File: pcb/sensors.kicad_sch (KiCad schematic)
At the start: 12 parts, among them J2 Conn_01x04_Pin, Q1 BSS138, Q2 BSS138, U3 BME280, U4 SGP30-2.5K

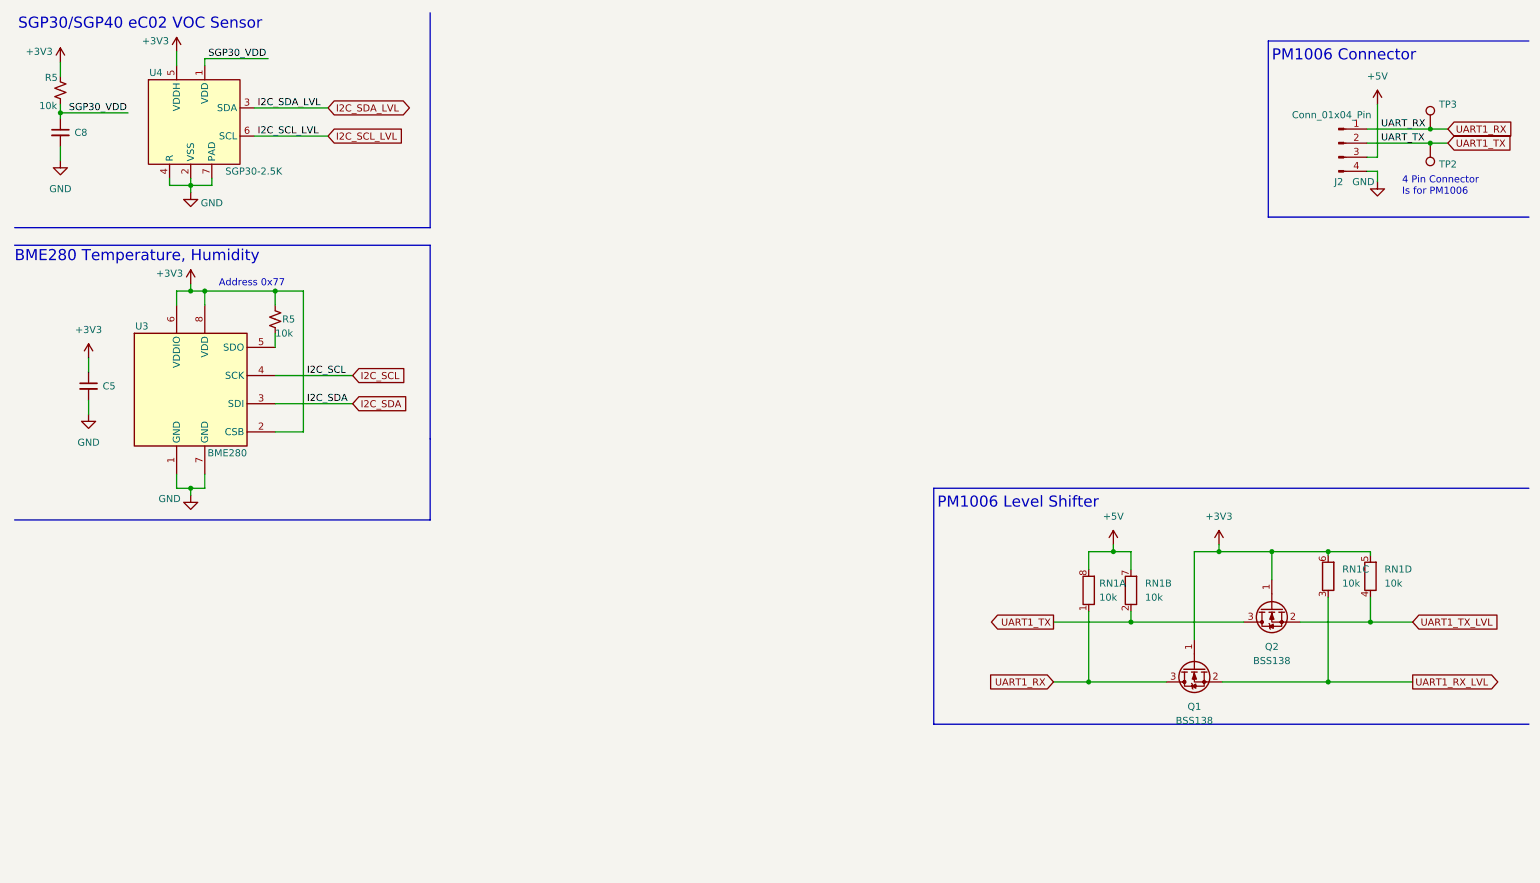
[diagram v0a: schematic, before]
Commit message: finish the routing need to move the esp32 up 5.5 mm
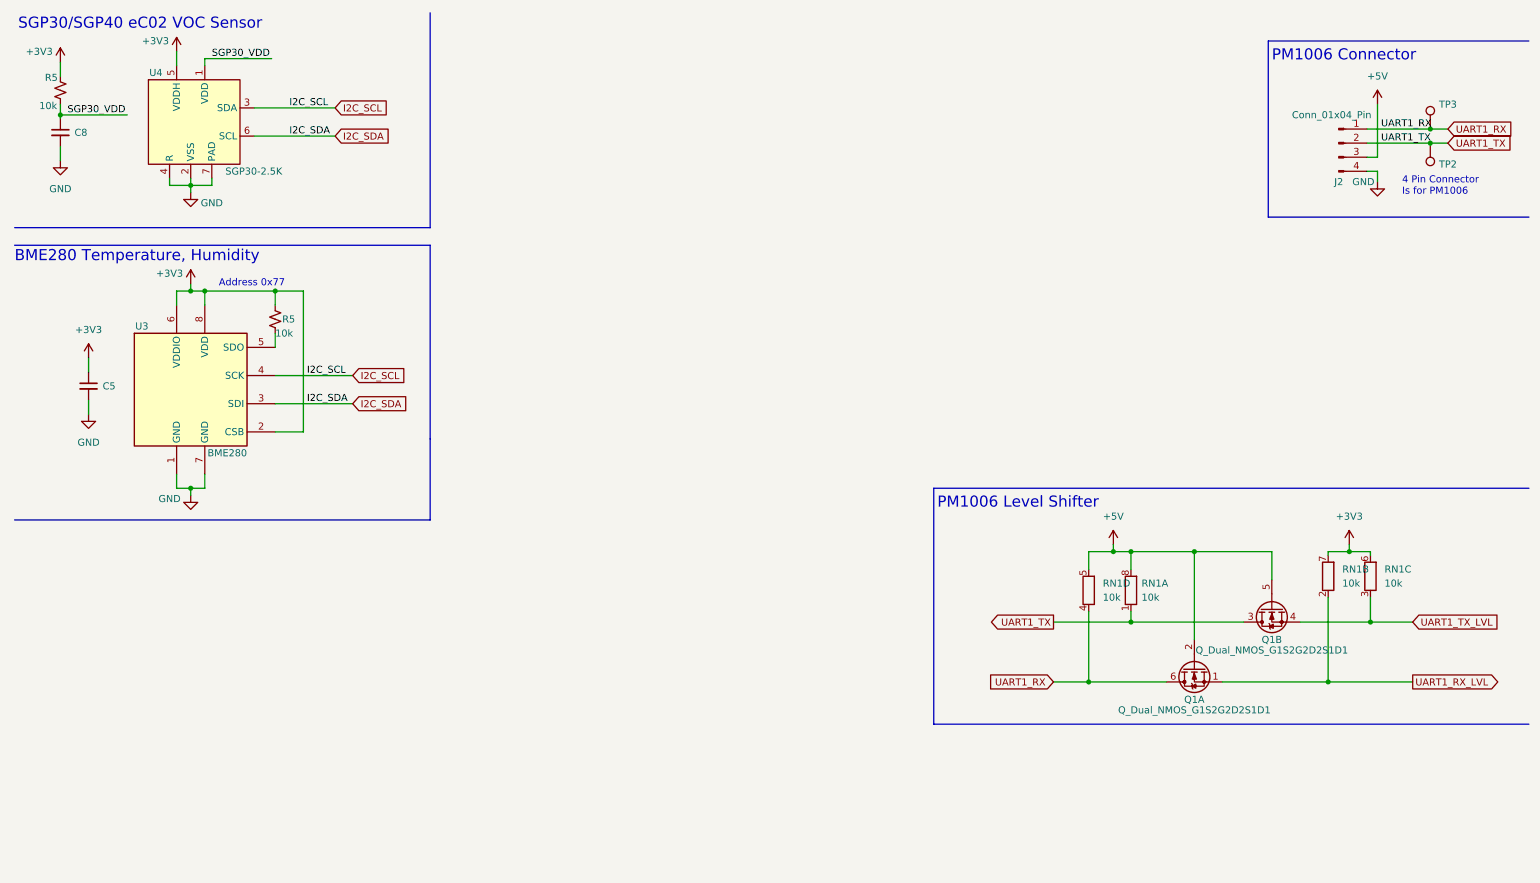
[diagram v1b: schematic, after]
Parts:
- removed Q1, Q2: BSS138, Package_TO_SOT_SMD:SOT-23, symbol Transistor_FET:BSS138
- added Q1: Q_Dual_NMOS_G1S2G2D2S1D1, Package_TO_SOT_SMD:SOT-363_SC-70-6, symbol Kevin_Lutzer_Lbr:Q_Dual_NMOS_BSS138PS
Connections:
- net I2C_SCL_LVL is gone; now on net I2C_SDA: U4.6 (SCL)
- net I2C_SDA_LVL is gone; now on net I2C_SCL: U4.3 (SDA)
- net +3V3: now also RN1.7 (R2.2); no longer RN1.5 (R4.2)
- net +5V: now also RN1.5 (R4.2), Q1.2 (G), Q1.5 (G); no longer RN1.7 (R2.2)
- net UART1_RX: now also RN1.4 (R4.1), Q1.6 (D); no longer RN1.1 (R1.1)
- net UART1_RX_LVL: now also RN1.2 (R2.1), Q1.1 (S); no longer RN1.3 (R3.1)
- net UART1_TX: now also RN1.1 (R1.1), Q1.3 (D); no longer RN1.2 (R2.1)
- net UART1_TX_LVL: now also RN1.3 (R3.1), Q1.4 (S); no longer RN1.4 (R4.1)
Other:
- moved on the sheet: RN1A, RN1B, RN1C, RN1D

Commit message: finish routing the PCB
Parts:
- U4: footprint Kevin_Lutzer_Lbr:SGP30-2.5K_SEN-M -> Kevin_Lutzer_Lbr:SGP30-2.5K_SEN
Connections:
- net +3V3: now also Q1.2 (G), Q1.5 (G)
- net +5V: no longer Q1.2 (G), Q1.5 (G)
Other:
- moved on the sheet: J2, Q1A, Q1B, RN1A, RN1B, RN1C, RN1D, TP2, TP3

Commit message: finish v4 and the images for doucmentation
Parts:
- removed Q1: Q_Dual_NMOS_G1S2G2D2S1D1, Package_TO_SOT_SMD:SOT-363_SC-70-6, symbol Kevin_Lutzer_Lbr:Q_Dual_NMOS_BSS138PS
- removed RN1: 10k, Resistor_SMD:R_Array_Concave_4x0603, symbol Device:R_Pack04_Split
- added C8: 0u1, Capacitor_SMD:C_0603_1608Metric, symbol Device:C_Small
- added D6: D_Photo, Diode_SMD:D_1206_3216Metric_Pad1.42x1.75mm_HandSolder, symbol Device:D_Photo
- added Q1: BSS138, Package_TO_SOT_SMD:SOT-23, symbol Transistor_FET:BSS138
- added R14: R_Small_US, Resistor_SMD:R_0603_1608Metric, symbol Device:R_Small_US
- added R5 (x2): 10k, Resistor_SMD:R_0603_1608Metric, symbol Device:R_Small_US
- added R5 (x2): 2k2, Resistor_SMD:R_0603_1608Metric, symbol Device:R_Small_US
- added R5 (x2): 0, Resistor_SMD:R_0603_1608Metric, symbol Device:R_Small_US
- C5, C8: value 100n -> 0u1
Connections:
- net +3V3: now also C8.1, Q1.1 (G), R14.2, R5.1, R5.2, R5.2
- net +5V: now also R5.1
- net GND: now also C8.2, D6.1 (K)
- net I2C_SCL: now also R5.1
- net I2C_SDA: now also R5.1
- net UART1_RX: now also R5.2; no longer J2.1 (Pin_1), TP3.1
- net UART1_TX: now also Q1.3 (D), R5.2, R5.2; no longer J2.2 (Pin_2), TP2.1
- net UART1_TX_LVL: now also Q1.2 (S), R5.2
- new net: J2.1 (Pin_1), R5.1, TP3.1
- new net: J2.2 (Pin_2), R5.1, TP2.1
- new net PD: D6.2 (A), R14.1
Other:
- note added: "For room reasons I only level shifted the TX signal so it can meet the 4.5V TTL Level of the sensor."
- note added: "I2C Pullups"
- note added: "Photo Diode"
- moved on the sheet: C8, R5, TP2, TP3

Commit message: cleanup undeeded pdf files and add gerbers
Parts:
- added C6: 1u, Capacitor_SMD:C_0603_1608Metric, symbol Device:C_Small
- J2: footprint Connector_JST:JST_ZE_BM04B-ZESS-TBT_1x04-1MP_P1.50mm_Vertical -> Kevin_Lutzer_Lbr:CONN_B4B-ZR-SM4-TF_JST
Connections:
- net +5V: now also C6.1
- net GND: now also C6.2
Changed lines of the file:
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@@
+    (stroke (width 0) (type default))
+  )
+  (wire (pts (xy 97.79 31.115) (xy 97.79 34.925))
     (stroke (width 0) (type default))
   )
@@
   )
   (wire (pts (xy 102.87 97.79) (xy 102.87 99.06))
+    (stroke (width 0) (type default))
+  )
+  (wire (pts (xy 97.79 23.495) (xy 97.79 26.035))
     (stroke (width 0) (type default))
   )
@@
     )
   )
+  (symbol (lib_id "power:+5V") (at 97.79 23.495 0) (unit 1)
+    (in_bom yes) (on_board yes) (dnp no) (fields_autoplaced)
+    (property "Reference" "#PWR033" (at 97.79 27.305 0)
+      (effects (font (size 1.27 1.27)) hide)
+    )
+    (property "Value" "+5V" (at 97.79 18.415 0)
+      (effects (font (size 1.27 1.27)))
+    )
+    (property "Footprint" "" (at 97.79 23.495 0)
+      (effects (font (size 1.27 1.27)) hide)
+    )
+    (property "Datasheet" "" (at 97.79 23.495 0)
+      (effects (font (size 1.27 1.27)) hide)
+    )
+    (pin "1")
+    (instances
+      (project "room_environment_monitor"
+        (path "/44f2386d-4dcf-411b-99dd-82c40d92c146"
+          (reference "#PWR033") (unit 1)
+        )
+        (path "/44f2386d-4dcf-411b-99dd-82c40d92c146/789efca6-28c5-460e-8523-846d22f060e4"
+          (reference "#PWR038") (unit 1)
+        )
+      )
+    )
+  )
   (symbol (lib_id "power:GND") (at 18.415 44.45 0) (unit 1)
     (in_bom yes) (on_board yes) (dnp no) (fields_autoplaced)
@@
     )
     (property "Value" "Conn_01x04_Pin" (at 101.6 25.4 0)
-      (effects (font (size 1.27 1.27)))
-    )
-    (property "Footprint" "Connector_JST:JST_ZE_BM04B-ZESS-TBT_1x04-1MP_P1.50mm_Vertical" (at 102.87 30.48 0)
+      (effects (font (size 1.27 1.27)) hide)
+    )
+    (property "Footprint" "Kevin_Lutzer_Lbr:CONN_B4B-ZR-SM4-TF_JST" (at 102.87 30.48 0)
       (effects (font (size 1.27 1.27)) hide)
     )
@@
         (path "/44f2386d-4dcf-411b-99dd-82c40d92c146/789efca6-28c5-460e-8523-846d22f060e4"
           (reference "D6") (unit 1)
+        )
+      )
+    )
+  )
+  (symbol (lib_id "power:GND") (at 97.79 34.925 0) (unit 1)
+    (in_bom yes) (on_board yes) (dnp no)
+    (property "Reference" "#PWR036" (at 97.79 41.275 0)
+      (effects (font (size 1.27 1.27)) hide)
+    )
+    (property "Value" "GND" (at 97.79 38.735 0)
+      (effects (font (size 1.27 1.27)))
+    )
+    (property "Footprint" "" (at 97.79 34.925 0)
+      (effects (font (size 1.27 1.27)) hide)
+    )
+    (property "Datasheet" "" (at 97.79 34.925 0)
+      (effects (font (size 1.27 1.27)) hide)
+    )
+    (pin "1")
+    (instances
+      (project "room_environment_monitor"
+        (path "/44f2386d-4dcf-411b-99dd-82c40d92c146"
+          (reference "#PWR036") (unit 1)
+        )
+        (path "/44f2386d-4dcf-411b-99dd-82c40d92c146/789efca6-28c5-460e-8523-846d22f060e4"
+          (reference "#PWR039") (unit 1)
         )
       )
@@
         )
       )
+    )
+  )
+  (symbol (lib_id "Device:C_Small") (at 97.79 28.575 0) (unit 1)
+    (in_bom yes) (on_board yes) (dnp no)
+    (property "Reference" "C6" (at 97.79 26.035 0)
+      (effects (font (size 1.27 1.27)) (justify left))
+    )
+    (property "Value" "1u" (at 97.79 31.115 0)
+      (effects (font (size 1.27 1.27)) (justify left))
+    )
+    (property "Footprint" "Capacitor_SMD:C_0603_1608Metric" (at 97.79 28.575 0)
+      (effects (font (size 1.27 1.27)) hide)
+    )
+    (property "Datasheet" "~" (at 97.79 28.575 0)
+      (effects (font (size 1.27 1.27)) hide)
+    )
+    (pin "1")
+    (pin "2")
+    (instances
+      (project "room_environment_monitor"
+        (path "/44f2386d-4dcf-411b-99dd-82c40d92c146"
+          (reference "C6") (unit 1)
+        )
+        (path "/44f2386d-4dcf-411b-99dd-82c40d92c146/789efca6-28c5-460e-8523-846d22f060e4"
+          (reference "C7") (unit 1)
+        )
+      )

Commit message: switch the sda and scl lines on the SGP40
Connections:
- net I2C_SCL: now also U4.6 (SCL); no longer U4.3 (SDA)
- net I2C_SDA: now also U4.3 (SDA); no longer U4.6 (SCL)
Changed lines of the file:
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@@
+    (stroke (width 0) (type default))
+  )
+  (wire (pts (xy 55.245 29.21) (xy 65.405 29.21))
+    (stroke (width 0) (type default))
+  )
+  (wire (pts (xy 42.545 125.095) (xy 42.545 127))
+    (stroke (width 0) (type default))
+  )
+  (wire (pts (xy 95.885 58.42) (xy 95.885 60.325))
+    (stroke (width 0) (type default))
+  )
+  (wire (pts (xy 120.015 30.48) (xy 132.08 30.48))
+    (stroke (width 0) (type default))
+  )
+  (wire (pts (xy 40.005 43.18) (xy 43.815 43.18))
+    (stroke (width 0) (type default))
+  )
+  (wire (pts (xy 18.415 36.195) (xy 18.415 36.83))
+    (stroke (width 0) (type default))
+  )
+  (wire (pts (xy 41.275 62.23) (xy 43.815 62.23))
+    (stroke (width 0) (type default))
+  )
+  (polyline (pts (xy 137.16 43.815) (xy 90.17 43.815))
+    (stroke (width 0) (type default))
+  )
+  (wire (pts (xy 47.625 43.18) (xy 47.625 41.91))
+    (stroke (width 0) (type default))
+  )
+  (polyline (pts (xy 12.065 53.975) (xy 86.995 53.975))
+    (stroke (width 0) (type default))
+  )
+  (wire (pts (xy 46.355 95.25) (xy 46.355 97.79))
+    (stroke (width 0) (type default))
+  )
+  (wire (pts (xy 46.355 127) (xy 42.545 127))
+    (stroke (width 0) (type default))
+  )
+  (polyline (pts (xy 90.17 46.99) (xy 125.095 46.99))
+    (stroke (width 0) (type default))
+  )
+  (wire (pts (xy 41.275 97.79) (xy 43.815 97.79))
+    (stroke (width 0) (type default))
+  )
+  (wire (pts (xy 46.355 128.905) (xy 46.355 127))
+    (stroke (width 0) (type default))
+  )
+  (wire (pts (xy 28.575 133.985) (xy 28.575 137.795))
+    (stroke (width 0) (type default))
+  )
+  (wire (pts (xy 59.055 77.47) (xy 73.025 77.47))
+    (stroke (width 0) (type default))
+  )
+  (wire (pts (xy 42.545 127) (xy 38.1 127))
+    (stroke (width 0) (type default))
+  )
+  (polyline (pts (xy 90.17 78.74) (xy 90.17 115.57))
+    (stroke (width 0) (type default))
+  )
+  (wire (pts (xy 120.015 27.94) (xy 132.08 27.94))
+    (stroke (width 0) (type default))
+  )
+  (wire (pts (xy 18.415 36.195) (xy 30.48 36.195))
+    (stroke (width 0) (type default))
+  )
+  (wire (pts (xy 30.48 20.32) (xy 41.275 20.32))
+    (stroke (width 0) (type default))
+  )
+  (wire (pts (xy 59.055 82.55) (xy 73.025 82.55))
+    (stroke (width 0) (type default))
+  )
+  (wire (pts (xy 107.95 30.48) (xy 111.76 30.48))
+    (stroke (width 0) (type default))
+  )
+  (wire (pts (xy 30.48 20.955) (xy 30.48 20.32))
+    (stroke (width 0) (type default))
+  )
+  (wire (pts (xy 102.87 90.17) (xy 102.87 92.71))
+    (stroke (width 0) (type default))
+  )
+  (wire (pts (xy 43.815 97.79) (xy 43.815 99.06))
+    (stroke (width 0) (type default))
+  )
+  (wire (pts (xy 46.355 137.795) (xy 51.435 137.795))
+    (stroke (width 0) (type default))
+  )
+  (polyline (pts (xy 145.415 12.065) (xy 137.16 12.065))
+    (stroke (width 0) (type default))
+  )
+  (wire (pts (xy 113.665 67.31) (xy 102.235 67.31))
+    (stroke (width 0) (type default))
+  )
+  (wire (pts (xy 46.355 62.23) (xy 43.815 62.23))
+    (stroke (width 0) (type default))
+  )
+  (wire (pts (xy 111.76 27.94) (xy 114.935 27.94))
+    (stroke (width 0) (type default))
+  )
+  (wire (pts (xy 102.87 99.06) (xy 107.95 99.06))
+    (stroke (width 0) (type default))
+  )
+  (polyline (pts (xy 145.415 43.815) (xy 145.415 12.065))
+    (stroke (width 0) (type default))
+  )
+  (wire (pts (xy 28.575 125.095) (xy 28.575 128.905))
+    (stroke (width 0) (type default))
+  )
+  (wire (pts (xy 18.415 34.29) (xy 18.415 36.195))
+    (stroke (width 0) (type default))
+  )
+  (wire (pts (xy 102.87 107.95) (xy 102.87 110.49))
+    (stroke (width 0) (type default))
+  )
+  (wire (pts (xy 18.415 26.67) (xy 18.415 29.21))
     (stroke (width 0) (type default))
   )
   (wire (pts (xy 55.245 34.29) (xy 65.405 34.29))
-    (stroke (width 0) (type default))
-  )
-  (wire (pts (xy 42.545 125.095) (xy 42.545 127))
-    (stroke (width 0) (type default))
-  )
-  (wire (pts (xy 95.885 58.42) (xy 95.885 60.325))
-    (stroke (width 0) (type default))
-  )
-  (wire (pts (xy 120.015 30.48) (xy 132.08 30.48))
-    (stroke (width 0) (type default))
-  )
-  (wire (pts (xy 40.005 43.18) (xy 43.815 43.18))
-    (stroke (width 0) (type default))
-  )
-  (wire (pts (xy 18.415 36.195) (xy 18.415 36.83))
-    (stroke (width 0) (type default))
-  )
-  (wire (pts (xy 41.275 62.23) (xy 43.815 62.23))
-    (stroke (width 0) (type default))
-  )
-  (polyline (pts (xy 137.16 43.815) (xy 90.17 43.815))
-    (stroke (width 0) (type default))
-  )
-  (wire (pts (xy 47.625 43.18) (xy 47.625 41.91))
-    (stroke (width 0) (type default))
-  )
-  (polyline (pts (xy 12.065 53.975) (xy 86.995 53.975))
-    (stroke (width 0) (type default))
-  )
-  (wire (pts (xy 46.355 95.25) (xy 46.355 97.79))
-    (stroke (width 0) (type default))
-  )
-  (wire (pts (xy 46.355 127) (xy 42.545 127))
-    (stroke (width 0) (type default))
-  )
-  (polyline (pts (xy 90.17 46.99) (xy 125.095 46.99))
-    (stroke (width 0) (type default))
-  )
-  (wire (pts (xy 41.275 97.79) (xy 43.815 97.79))
-    (stroke (width 0) (type default))
-  )
-  (wire (pts (xy 46.355 128.905) (xy 46.355 127))
-    (stroke (width 0) (type default))
-  )
-  (wire (pts (xy 28.575 133.985) (xy 28.575 137.795))
-    (stroke (width 0) (type default))
-  )
-  (wire (pts (xy 59.055 77.47) (xy 73.025 77.47))
-    (stroke (width 0) (type default))
-  )
-  (wire (pts (xy 42.545 127) (xy 38.1 127))
-    (stroke (width 0) (type default))
-  )
-  (polyline (pts (xy 90.17 78.74) (xy 90.17 115.57))
-    (stroke (width 0) (type default))
-  )
-  (wire (pts (xy 120.015 27.94) (xy 132.08 27.94))
-    (stroke (width 0) (type default))
-  )
-  (wire (pts (xy 18.415 36.195) (xy 30.48 36.195))
-    (stroke (width 0) (type default))
-  )
-  (wire (pts (xy 30.48 20.32) (xy 41.275 20.32))
-    (stroke (width 0) (type default))
-  )
-  (wire (pts (xy 59.055 82.55) (xy 73.025 82.55))
-    (stroke (width 0) (type default))
-  )
-  (wire (pts (xy 107.95 30.48) (xy 111.76 30.48))
-    (stroke (width 0) (type default))
-  )
-  (wire (pts (xy 30.48 20.955) (xy 30.48 20.32))
-    (stroke (width 0) (type default))
-  )
-  (wire (pts (xy 102.87 90.17) (xy 102.87 92.71))
-    (stroke (width 0) (type default))
-  )
-  (wire (pts (xy 43.815 97.79) (xy 43.815 99.06))
-    (stroke (width 0) (type default))
-  )
-  (wire (pts (xy 46.355 137.795) (xy 51.435 137.795))
-    (stroke (width 0) (type default))
-  )
-  (polyline (pts (xy 145.415 12.065) (xy 137.16 12.065))
-    (stroke (width 0) (type default))
-  )
-  (wire (pts (xy 113.665 67.31) (xy 102.235 67.31))
-    (stroke (width 0) (type default))
-  )
-  (wire (pts (xy 46.355 62.23) (xy 43.815 62.23))
-    (stroke (width 0) (type default))
-  )
-  (wire (pts (xy 111.76 27.94) (xy 114.935 27.94))
-    (stroke (width 0) (type default))
-  )
-  (wire (pts (xy 102.87 99.06) (xy 107.95 99.06))
-    (stroke (width 0) (type default))
-  )
-  (polyline (pts (xy 145.415 43.815) (xy 145.415 12.065))
-    (stroke (width 0) (type default))
-  )
-  (wire (pts (xy 28.575 125.095) (xy 28.575 128.905))
-    (stroke (width 0) (type default))
-  )
-  (wire (pts (xy 18.415 34.29) (xy 18.415 36.195))
-    (stroke (width 0) (type default))
-  )
-  (wire (pts (xy 102.87 107.95) (xy 102.87 110.49))
-    (stroke (width 0) (type default))
-  )
-  (wire (pts (xy 18.415 26.67) (xy 18.415 29.21))
-    (stroke (width 0) (type default))
-  )
-  (wire (pts (xy 55.245 29.21) (xy 65.405 29.21))
     (stroke (width 0) (type default))
   )
@@
     (effects (font (size 1.27 1.27)) (justify left bottom))
   )
-  (label "I2C_SCL" (at 56.515 29.21 0) (fields_autoplaced)
-    (effects (font (size 1.27 1.27)) (justify left bottom))
-  )
-  (label "I2C_SDA" (at 56.515 34.29 0) (fields_autoplaced)
+  (label "I2C_SCL" (at 56.515 34.29 0) (fields_autoplaced)
+    (effects (font (size 1.27 1.27)) (justify left bottom))
+  )
+  (label "I2C_SDA" (at 56.515 29.21 0) (fields_autoplaced)
     (effects (font (size 1.27 1.27)) (justify left bottom))
   )
@@
     )
   )
-  (global_label "I2C_SCL" (shape input) (at 65.405 29.21 0) (fields_autoplaced)
-    (effects (font (size 1.27 1.27)) (justify left))
-    (property "Intersheetrefs" "${INTERSHEET_REFS}" (at 75.9497 29.21 0)
+  (global_label "I2C_SCL" (shape input) (at 65.405 34.29 0) (fields_autoplaced)
+    (effects (font (size 1.27 1.27)) (justify left))
+    (property "Intersheetrefs" "${INTERSHEET_REFS}" (at 75.9497 34.29 0)
       (effects (font (size 1.27 1.27)) (justify left) hide)
     )
@@
     )
   )
-  (global_label "I2C_SDA" (shape input) (at 65.405 34.29 0) (fields_autoplaced)
-    (effects (font (size 1.27 1.27)) (justify left))
-    (property "Intersheetrefs" "${INTERSHEET_REFS}" (at 76.0102 34.29 0)
-      (effects (font (size 1.27 1.27)) (justify left) hide)
-    )
+  (global_label "I2C_SDA" (shape input) (at 65.405 29.21 0) (fields_autoplaced)
+    (effects (font (size 1.27 1.27)) (justify left))
+    (property "Intersheetrefs" "${INTERSHEET_REFS}" (at 76.0102 29.21 0)
+      (effects (font (size 1.27 1.27)) (justify left) hide)
+    )

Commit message: Use a 4.7 ohm resistor for the RC Filter on the VDD for SGP40
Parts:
- R5: value 10k -> 4.7
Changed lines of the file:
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@@
       (effects (font (size 1.27 1.27)) (justify left))
     )
-    (property "Value" "10k" (at 14.605 34.544 0)
+    (property "Value" "4.7" (at 14.605 34.544 0)
       (effects (font (size 1.27 1.27)) (justify left))
     )

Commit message: README
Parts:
- added JP1: SolderJumper_2_Open, Jumper:SolderJumper-2_P1.3mm_Open_RoundedPad1.0x1.5mm, symbol Jumper:SolderJumper_2_Open
- added Q2: BSS138, Package_TO_SOT_SMD:SOT-23, symbol Transistor_FET:BSS138
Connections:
- net GND: now also JP1.1 (A), Q2.2 (S); no longer J2.4 (Pin_4)
- new net: J2.4 (Pin_4), JP1.2 (B), Q2.3 (D)
- new net PM1006_EN: Q2.1 (G)
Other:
- moved on the sheet: C6, J2, R5, TP2, TP3
